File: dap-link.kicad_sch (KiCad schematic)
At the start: 53 parts, among them J1 Molex 0473460001, J2 SWD 6 PIN 2.54mm, J3 JTAG/SWD 10 pin 2.54mm, J4 JTAG/SWD 10 pin 1.27mm, J5 JTAG/SWD 20 PIN 1.27mm, J6 DAPLink Flash, Q1 MMBT3904, U1 SC573V33RTRC, U2 STM32F103CBTx, U3 150141SV73110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

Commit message: case v1
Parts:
- removed D5, D6: HSP051-4N10, MyLib:UQFN1.9x1_10L, symbol tvs_diodes:HSP051-4N10
- removed J2: SWD 6 PIN 2.54mm, Connector_PinHeader_2.54mm:PinHeader_1x06_P2.54mm_Vertical, symbol Connector:Conn_01x06_Male
- removed J5: JTAG/SWD 20 PIN 1.27mm, Connector_PinHeader_1.27mm:PinHeader_2x10_P1.27mm_Vertical_SMD, symbol Connector_Generic:Conn_02x10_Odd_Even
- removed J6: DAPLink Flash, MyLib:PinHeader_2x05_P1.27mm_Vertical_SMD, symbol Connector_Generic:Conn_02x05_Odd_Even
- removed R16, R17: 22R, Resistor_SMD:R_0603_1608Metric, symbol Device:R_Small
- removed R6: 10k, Resistor_SMD:R_0603_1608Metric, symbol Device:R_Small
- added J2: Conn_01x05_Male, MyLib:SWD_SOLDER, symbol Connector:Conn_01x05_Male
- J3: value JTAG/SWD 10 pin 2.54mm -> SWD 10 pin 2.54mm
- J4: value JTAG/SWD 10 pin 1.27mm -> SWD 10 pin 1.27mm
- U3: footprint SMT_V73110_WRE -> MyLib:150141SV73110; symbol 2023-01-20_13-48-14:150141SV73110 -> dap_link_led:150141SV73110
- Y1: footprint Crystal:Crystal_SMD_HC49-SD -> MyLib:ECS-023G
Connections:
- net T_JTMS is gone; now on net T_SWDIO_IN: R14.2, R3.2, U2.25 (PB12)
- net +3V3: now also J2.1 (Pin_1); no longer U2.39 (PB3)
- net GND: now also R5.1, J2.5 (Pin_5); no longer R5.2, U2.20 (PB2), U2.28 (PB15), U2.29 (PA8)
- net STM_NRST: now also J2.4 (Pin_4)
- net STM_SWCLK: now also J2.3 (Pin_3)
- net STM_SWDIO: now also J2.2 (Pin_2)
- net T_SWDIO_IN: no longer R3.1, U2.27 (PB14)
- net VTREF: now also D7.1 (IO1)
- net at U2.2 (PC13): no longer R5.1
- net BOOT0: now reaches R4.2, U2.44 (BOOT0)
- net LED renamed COM_LED
- net COM_LED: no longer R10.1
- removed net SWO: D7.1 (IO1), J3.6 (Pin_6), J4.6 (Pin_6)
- net TCLK renamed SWCLK
- removed net TDI: D7.3 (IO3), J3.8 (Pin_8), J4.8 (Pin_8)
- net TMS renamed SWDIO
- net SWDIO: now also D7.3 (IO3)
- net T_JTCK renamed T_SWCLK
- net T_SWCLK: no longer U2.15 (PA5)
- net T_JTDI: no longer names the net of U2.17 (PA7)
- net T_JTDO: no longer names the net of U2.16 (PA6)
- net T_SWO: no longer names the net of U2.31 (PA10)
- new net BOOT1: R5.2, U2.20 (PB2)
- new net CONNECTED_LED: R10.1, U2.29 (PA8)
- new net POWER_EN_LED: U2.28 (PB15)
- new net T_SWDIO_OUT: R3.1, U2.27 (PB14)
- no-connect marks 26 -> 28
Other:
- moved on the sheet: R10, R13, R14, R15, R2, R3, R4, U3

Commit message: changes
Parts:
- added J5: TC2050-IDC, MyLib:TAG-CONNECT_TC2050-IDC, symbol TC2050-IDC:TC2050-IDC
- C2, C3: value 20p -> 18p
- D1, D2, D3: value D_Small -> SM5817PL-TP; footprint Diode_SMD:Nexperia_CFP3_SOD-123W -> Diode_SMD:D_SOD-123
- D4, D7: DK-PN (none) -> 497-15060-1-ND
- D5: renamed from U3; symbol dap_link_led:150141SV73110 -> 150141SV73110:150141SV73110; DK-PN (none) -> 732-13404-1-ND
- J3: DK-PN 609-4950-ND -> 1175-1621-ND
- J4: DK-PN 1175-1735-ND -> 609-4054-ND
- Q1: DK-PN (none) -> 4530-MMBT3904CT-ND
- U1: footprint SC_33RTRC_SEM -> MyLib:SC573V33RTRC; DK-PN (none) -> SC573V33RTRCCT-ND
- U2: DK-PN (none) -> 497-17380-1-ND
- Y1: DK-PN (none) -> XC2340CT-ND
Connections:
- net +3V3: now also J5.1
- net CONNECTED_LED: now also U2.42 (PB6); no longer U2.29 (PA8)
- net GND: now also J5.2, J5.3, J5.4, J5.5
- net STM_NRST: now also J5.6
- net STM_SWCLK: now also J5.9
- net STM_SWDIO: now also J5.10
- net T_VTREF: now reaches D1.1 (K), R9.2
- no-connect marks 28 -> 30
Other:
- note added: "MCU BYPASS"
- note added: "POWER"
- note added: "STATUS LED"
- note added: "SWD IN"
- note added: "SWD OUT"
- note added: "USB"
- note added: "VTREF SELECTION"
- moved on the sheet: C1, C10, C2, C3, C4, C5, C6, C7, C8, C9, D1, D2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

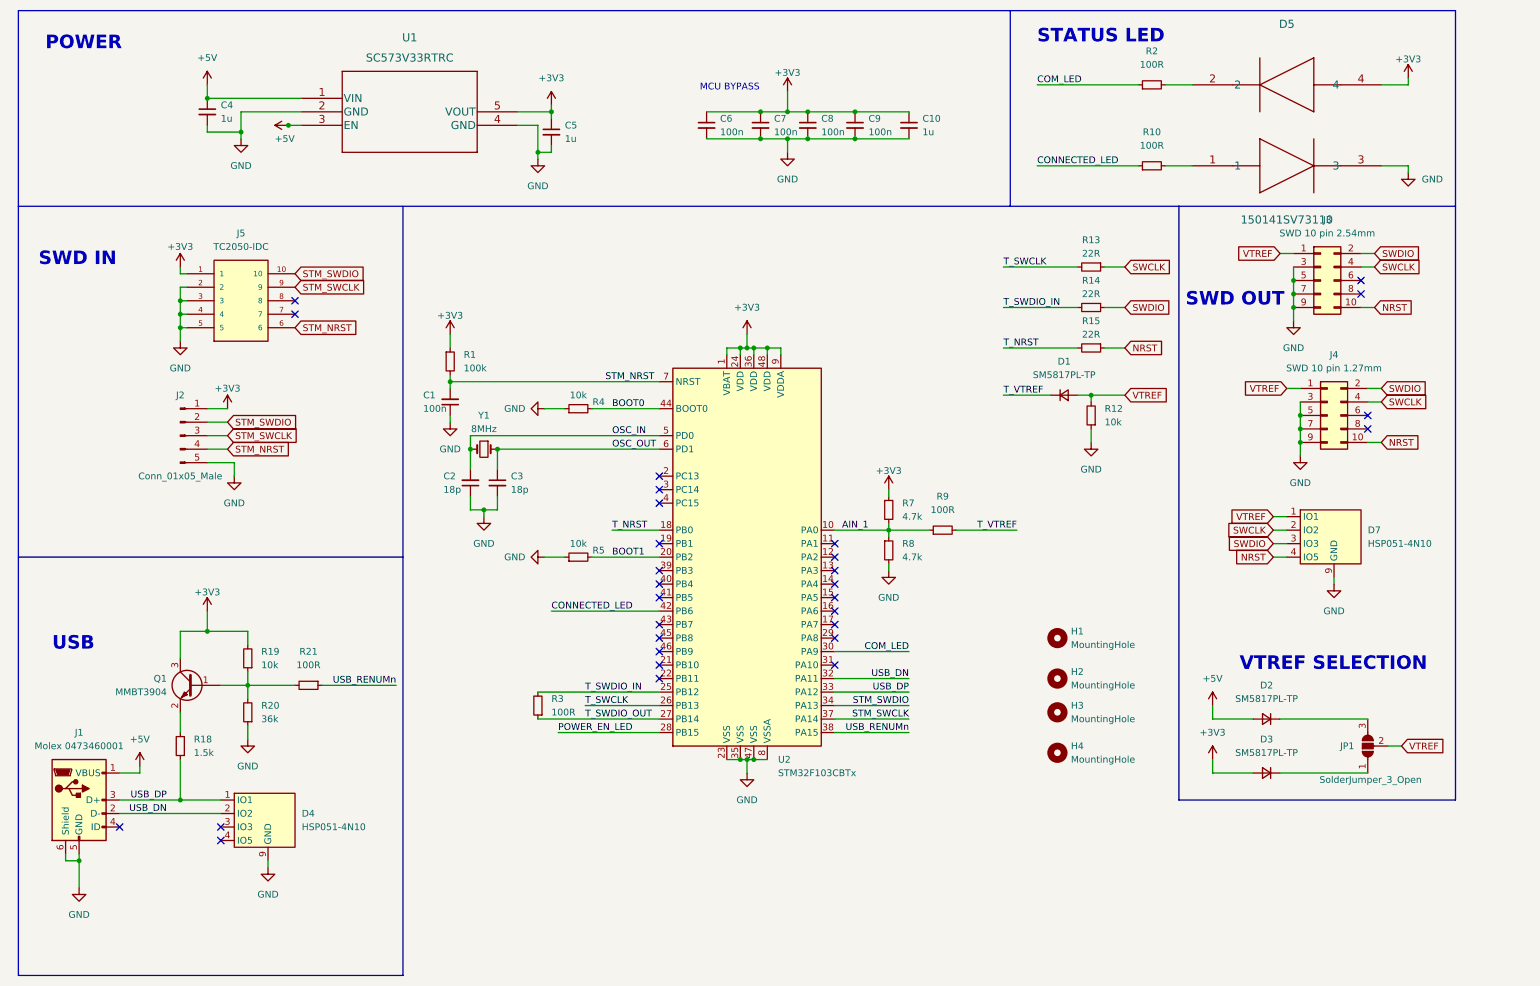
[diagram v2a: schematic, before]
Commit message: changed 1.27mm swd out connector to horizontal orientation
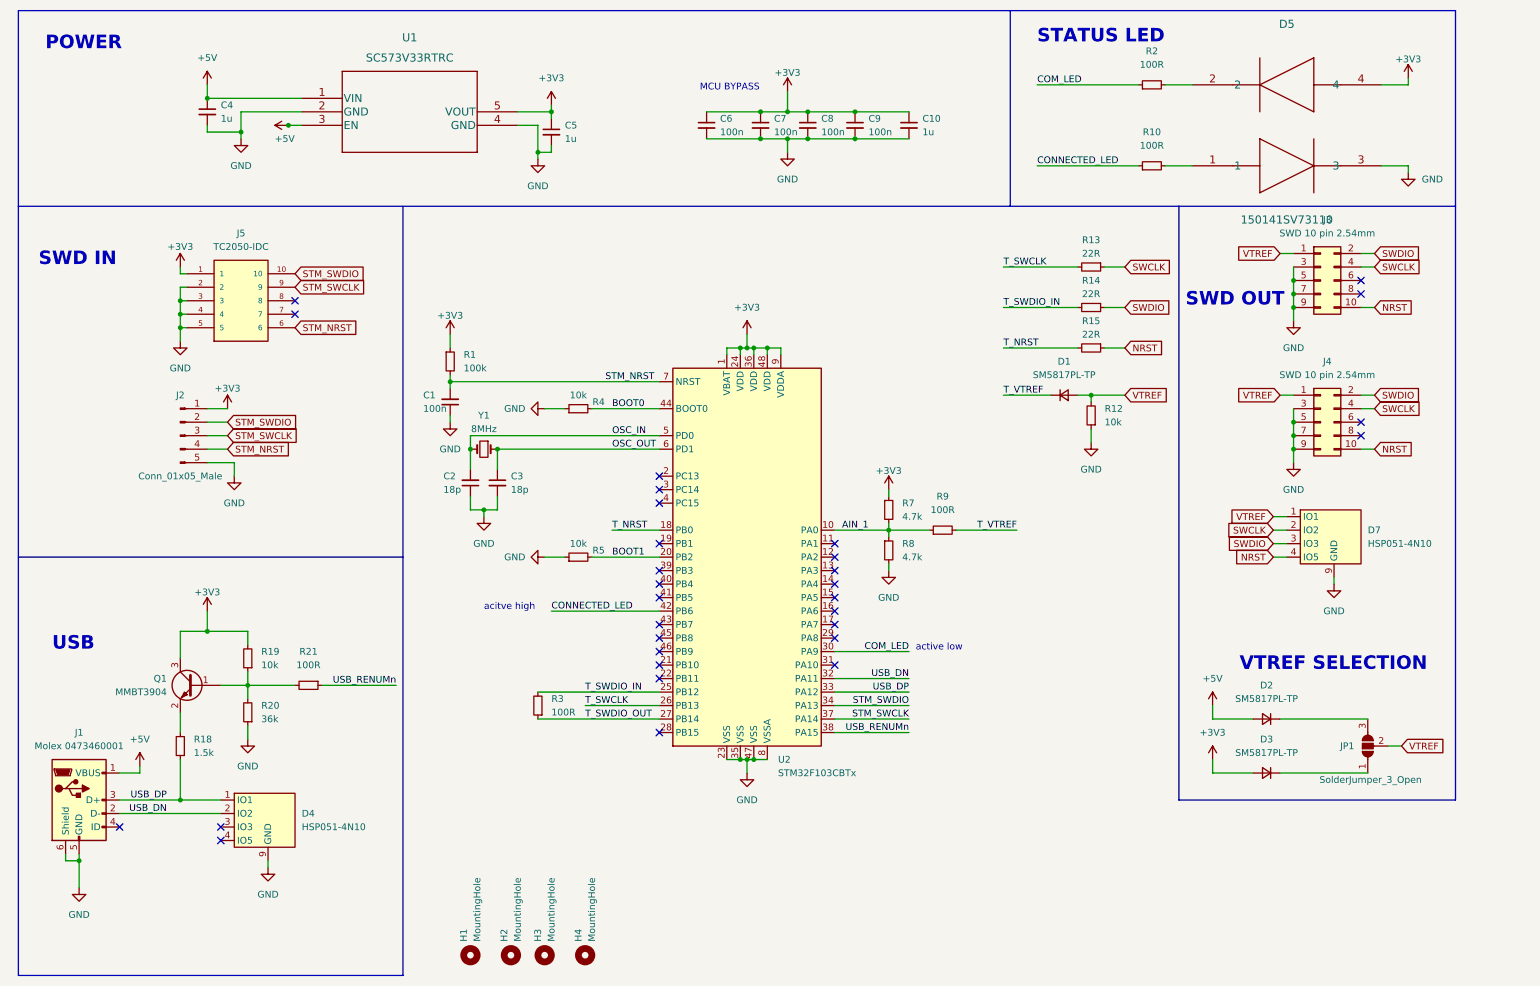
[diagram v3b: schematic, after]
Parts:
- J4: value SWD 10 pin 1.27mm -> SWD 10 pin 2.54mm; footprint MyLib:PinHeader_2x05_P1.27mm_Vertical_SMD -> MyLib:GBED204-0579B001C1AD; DK-PN 609-4054-ND -> 1175-1621-ND
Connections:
- net POWER_EN_LED: no longer names the net of U2.28 (PB15)
- no-connect marks 30 -> 31
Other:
- note added: "acitve high"
- note added: "active low"
- moved on the sheet: H1, H2, H3, H4
